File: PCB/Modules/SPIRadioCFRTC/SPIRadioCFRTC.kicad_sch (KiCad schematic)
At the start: 26 parts, among them J1 In, J2 Micro_SD_Card_Det_9pin, Q1 Q_NMOS_GSD, Q2 Q_NMOS_GSD, Q3 Q_NMOS_GSD, U1 DS1390U, U2 nRF24L01P_Module, U3 AMS1117-3.3, Y1 32.767kHz

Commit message: Convert all KiCad to 6.0, clean up libraries, remove files that shouldn't be committed.
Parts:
- J2: symbol SPIRadioCFRTC:Micro_SD_Card_Det_9pin -> KTANE:Micro_SD_Card_Det_9pin
- U1: symbol SPIRadioCFRTC:DS1390U -> KTANE:DS1390U
- U2: symbol SPIRadioCFRTC:nRF24L01P_Module -> KTANE:nRF24L01P_Module
- U3: footprint Package_TO_SOT_SMD:SOT-23 -> Package_TO_SOT_SMD:SOT-223-3_TabPin2
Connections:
- net +3V3 renamed +3.3V
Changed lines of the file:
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@@
     (pin "2")
   )
-  (symbol (lib_id "power:+3.3V") (at 189.23 23.114 0) (unit 1)
+  (symbol (lib_name "+3.3V_2") (lib_id "power:+3.3V") (at 189.23 23.114 0) (unit 1)
     (in_bom yes) (on_board yes)
     (property "Reference" "#PWR01" (id 0) (at 189.23 26.924 0)
@@
     (pin "2")
   )
-  (symbol (lib_id "power:+3.3V") (at 262.89 52.705 0) (mirror y) (unit 1)
+  (symbol (lib_name "+3.3V_8") (lib_id "power:+3.3V") (at 262.89 52.705 0) (mirror y) (unit 1)
     (in_bom yes) (on_board yes)
     (property "Reference" "#PWR014" (id 0) (at 262.89 56.515 0)
@@
     (pin "1")
   )
-  (symbol (lib_id "power:+3.3V") (at 85.852 86.36 0) (mirror y) (unit 1)
+  (symbol (lib_name "+3.3V_1") (lib_id "power:+3.3V") (at 85.852 86.36 0) (mirror y) (unit 1)
     (in_bom yes) (on_board yes)
     (property "Reference" "#PWR028" (id 0) (at 85.852 90.17 0)
@@
     (property "Reference" "U3" (id 0) (at 113.03 77.9485 0))
     (property "Value" "AMS1117-3.3" (id 1) (at 113.03 80.7236 0))
-    (property "Footprint" "Package_TO_SOT_SMD:SOT-23" (id 2) (at 113.03 78.74 0)
+    (property "Footprint" "Package_TO_SOT_SMD:SOT-223-3_TabPin2" (id 2) (at 113.03 78.74 0)
       (effects (font (size 1.27 1.27)) hide)
     )
@@
     (pin "1")
   )
-  (symbol (lib_id "SPIRadioCFRTC:Micro_SD_Card_Det_9pin") (at 49.53 91.44 0) (mirror y) (unit 1)
+  (symbol (lib_id "KTANE:Micro_SD_Card_Det_9pin") (at 49.53 91.44 0) (mirror y) (unit 1)
     (in_bom yes) (on_board yes) (fields_autoplaced)
     (property "Reference" "J2" (id 0) (at 48.895 70.9635 0))
@@
     (pin "1")
   )
-  (symbol (lib_id "power:+3.3V") (at 82.55 24.13 0) (unit 1)
+  (symbol (lib_name "+3.3V_7") (lib_id "power:+3.3V") (at 82.55 24.13 0) (unit 1)
     (in_bom yes) (on_board yes)
     (property "Reference" "#PWR04" (id 0) (at 82.55 27.94 0)
@@
     (pin "3")
   )
-  (symbol (lib_id "SPIRadioCFRTC:nRF24L01P_Module") (at 189.23 39.37 0) (unit 1)
+  (symbol (lib_id "KTANE:nRF24L01P_Module") (at 189.23 39.37 0) (unit 1)
     (in_bom yes) (on_board yes) (fields_autoplaced)
     (property "Reference" "U2" (id 0) (at 191.2494 25.2943 0)
@@
     (pin "1")
   )
-  (symbol (lib_id "power:+3.3V") (at 20.32 78.74 0) (unit 1)
+  (symbol (lib_name "+3.3V_4") (lib_id "power:+3.3V") (at 20.32 78.74 0) (unit 1)
     (in_bom yes) (on_board yes)
     (property "Reference" "#PWR018" (id 0) (at 20.32 82.55 0)
@@
     (pin "2")
   )
-  (symbol (lib_id "power:+3.3V") (at 262.89 25.4 0) (mirror y) (unit 1)
+  (symbol (lib_name "+3.3V_9") (lib_id "power:+3.3V") (at 262.89 25.4 0) (mirror y) (unit 1)
     (in_bom yes) (on_board yes)
     (property "Reference" "#PWR07" (id 0) (at 262.89 29.21 0)
@@
     (pin "1")
   )
-  (symbol (lib_id "power:+3.3V") (at 156.21 78.74 0) (unit 1)
+  (symbol (lib_name "+3.3V_14") (lib_id "power:+3.3V") (at 156.21 78.74 0) (unit 1)
     (in_bom yes) (on_board yes)
     (property "Reference" "#PWR021" (id 0) (at 156.21 82.55 0)
@@
     (pin "1")
   )
-  (symbol (lib_id "power:+3.3V") (at 162.56 78.74 0) (unit 1)
+  (symbol (lib_name "+3.3V_11") (lib_id "power:+3.3V") (at 162.56 78.74 0) (unit 1)
     (in_bom yes) (on_board yes)
     (property "Reference" "#PWR022" (id 0) (at 162.56 82.55 0)
@@
     (pin "2")
   )
-  (symbol (lib_id "power:+3.3V") (at 151.13 26.67 0) (unit 1)
+  (symbol (lib_name "+3.3V_3") (lib_id "power:+3.3V") (at 151.13 26.67 0) (unit 1)
     (in_bom yes) (on_board yes)
     (property "Reference" "#PWR08" (id 0) (at 151.13 30.48 0)
@@
     (pin "1")
   )
-  (symbol (lib_id "SPIRadioCFRTC:DS1390U") (at 115.824 39.37 0) (unit 1)
+  (symbol (lib_id "KTANE:DS1390U") (at 115.824 39.37 0) (unit 1)
     (in_bom yes) (on_board yes) (fields_autoplaced)
     (property "Reference" "U1" (id 0) (at 117.8434 50.3587 0)
@@
     (pin "9")
   )
-  (symbol (lib_id "power:+3.3V") (at 143.51 78.74 0) (unit 1)
+  (symbol (lib_name "+3.3V_13") (lib_id "power:+3.3V") (at 143.51 78.74 0) (unit 1)
     (in_bom yes) (on_board yes)
     (property "Reference" "#PWR019" (id 0) (at 143.51 82.55 0)
@@
     (pin "2")
   )
-  (symbol (lib_id "power:+3.3V") (at 119.634 23.876 0) (unit 1)
+  (symbol (lib_name "+3.3V_6") (lib_id "power:+3.3V") (at 119.634 23.876 0) (unit 1)
     (in_bom yes) (on_board yes)
     (property "Reference" "#PWR03" (id 0) (at 119.634 27.686 0)
@@
     (pin "2")
   )
-  (symbol (lib_id "power:+3.3V") (at 149.86 78.74 0) (unit 1)
+  (symbol (lib_name "+3.3V_12") (lib_id "power:+3.3V") (at 149.86 78.74 0) (unit 1)
     (in_bom yes) (on_board yes)
     (property "Reference" "#PWR020" (id 0) (at 149.86 82.55 0)
@@
     (pin "2")
   )
-  (symbol (lib_id "power:+3.3V") (at 125.73 81.28 0) (unit 1)
+  (symbol (lib_name "+3.3V_10") (lib_id "power:+3.3V") (at 125.73 81.28 0) (unit 1)
     (in_bom yes) (on_board yes)
     (property "Reference" "#PWR027" (id 0) (at 125.73 85.09 0)
@@
     (pin "2")
   )
-  (symbol (lib_id "power:+3.3V") (at 262.89 80.01 0) (mirror y) (unit 1)
+  (symbol (lib_name "+3.3V_5") (lib_id "power:+3.3V") (at 262.89 80.01 0) (mirror y) (unit 1)
     (in_bom yes) (on_board yes)
     (property "Reference" "#PWR025" (id 0) (at 262.89 83.82 0)
@@
     )
     (path "/245afab8-87c2-4797-af78-aa00d5229c94"
-      (reference "U3") (unit 1) (value "AMS1117-3.3") (footprint "Package_TO_SOT_SMD:SOT-23")
+      (reference "U3") (unit 1) (value "AMS1117-3.3") (footprint "Package_TO_SOT_SMD:SOT-223-3_TabPin2")
     )
     (path "/8f7320f7-8fdb-4e68-b345-a40e837bd78d"

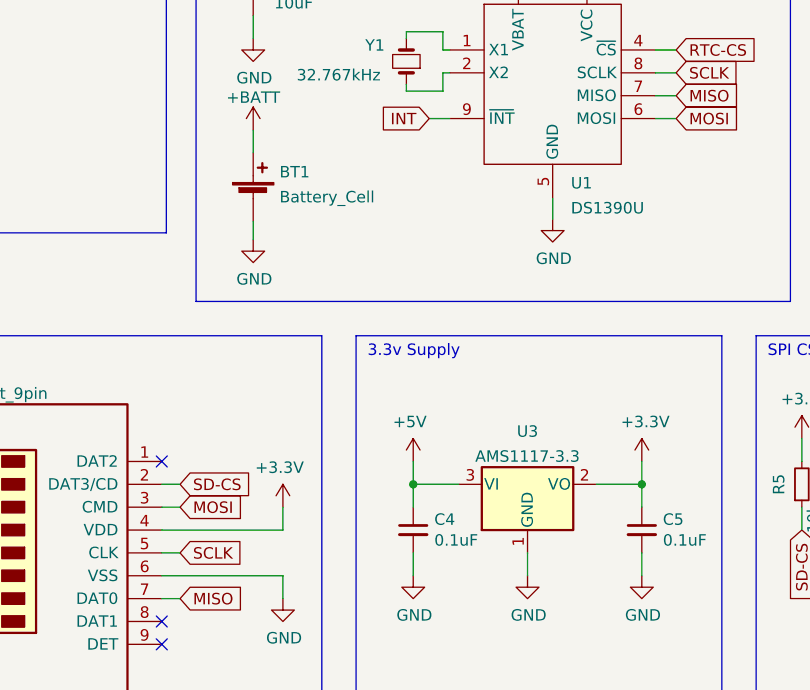
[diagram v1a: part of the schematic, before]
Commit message: Upgrade KiCad files from 6.0 to 7.0.
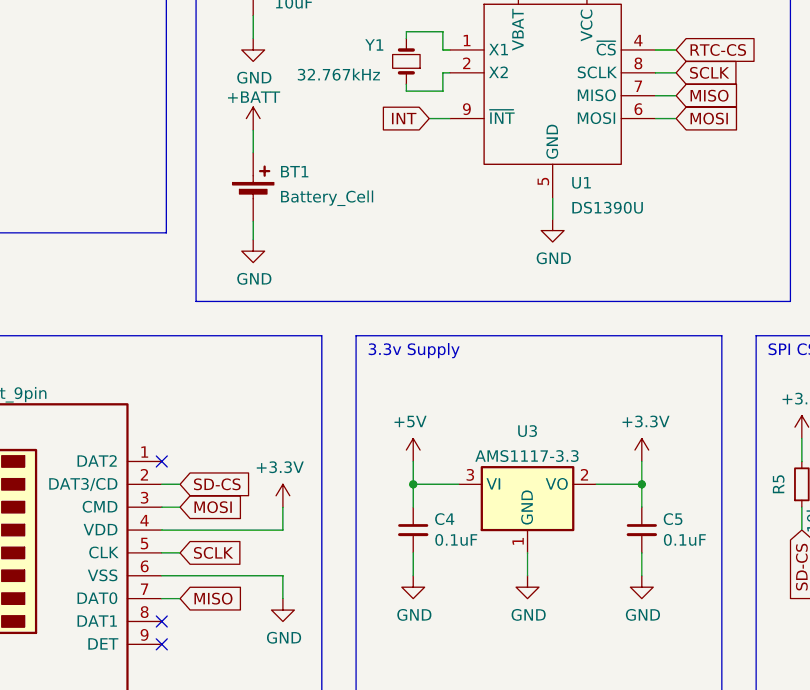
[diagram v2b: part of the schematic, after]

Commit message: First pass of PCB rework.
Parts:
- removed C3: 10uF, Capacitor_SMD:C_0805_2012Metric, symbol Device:C_Small
- removed J2: Micro_SD_Card_Det_9pin, SPIRadioCFRTC:mSDCardSlot, symbol KTANE:Micro_SD_Card_Det_9pin
- removed Q1, Q2, Q3: Q_NMOS_GSD, Package_TO_SOT_SMD:SOT-23, symbol Device:Q_NMOS_GSD
- removed R10, R11, R2, R3, R4, R5, R6, R7, R8, R9: 10k, Resistor_SMD:R_0805_2012Metric, symbol Device:R_Small
- removed U3: AMS1117-3.3, Package_TO_SOT_SMD:SOT-223-3_TabPin2, symbol Regulator_Linear:AMS1117-3.3
- added C6: 10uF, Capacitor_SMD:C_0603_1608Metric, symbol Device:C_Small
- added C7: 0.1uF, Capacitor_SMD:C_0603_1608Metric, symbol Device:C_Small
- added H1: MountingHole, MountingHole:MountingHole_3.2mm_M3, symbol Mechanical:MountingHole
- added J2: ESP32, Connector:Tag-Connect_TC2030-IDC-NL_2x03_P1.27mm_Vertical, symbol Connector_Generic:Conn_02x03_Odd_Even
- added U4: ESP32-WROOM-32, RF_Module:ESP32-WROOM-32U, symbol RF_Module:ESP32-WROOM-32U
- BT1: footprint SPIRadioCFRTC:CellHolder -> KTANE:CellHolder
- C1, C2: footprint Capacitor_SMD:C_0805_2012Metric -> Capacitor_SMD:C_0603_1608Metric
- C4: value 0.1uF -> 22uF; footprint Capacitor_SMD:C_0805_2012Metric -> Capacitor_SMD:C_0603_1608Metric
- C5: value 0.1uF -> 47uF; footprint Capacitor_SMD:C_0805_2012Metric -> Capacitor_SMD:C_0603_1608Metric
- J1: footprint Custom:PinHeader_2x08_P2.54mm_Vertical-Centered -> KTANE:PinHeader_2x08_P2.54mm_Vertical-Centered
- R1: footprint Resistor_SMD:R_0805_2012Metric -> Resistor_SMD:R_0603_1608Metric
- U2: footprint SPIRadioCFRTC:NRF24L01P-Module -> KTANE:NRF24L01P-Module
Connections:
- net IN-MISO is gone; now on net +5V: J1.2 (Pin_2)
- net IN-MOSI is gone; now on net +3.3V: J1.4 (Pin_4)
- net SD-CS is gone; now on net SPI-CIPO: J1.14 (Pin_14)
- net +3.3V: now also C4.1, R1.1, C7.1, J2.2 (Pin_2), U4.2 (VDD)
- net +5V: no longer C4.1, J1.11 (Pin_11), J1.13 (Pin_13), J1.15 (Pin_15), J1.9 (Pin_9), R1.2
- net GND: now also J1.16 (Pin_16), C6.2, C7.2, J2.3 (Pin_3), U4.1 (GND), U4.15 (GND), U4.38 (GND), U4.39 (GND); no longer J1.1 (Pin_1), J1.3 (Pin_3), J1.5 (Pin_5), J1.7 (Pin_7)
- net NF24-CE: now also J1.7 (Pin_7); no longer J1.10 (Pin_10)
- net NF24-CS: now also J1.5 (Pin_5); no longer J1.12 (Pin_12)
- net RTC-CS: now also J1.1 (Pin_1); no longer J1.16 (Pin_16)
- net IN-SCLK renamed I2C-CLK
- net I2C-CLK: no longer R1.1
- removed net INT: J1.8 (Pin_8), U1.9 (~{INT}), U2.7 (~{IRQ})
- net MISO renamed SPI-CIPO
- net SPI-CIPO: now also U4.14 (IO12)
- net MOSI renamed SPI-COPI
- net SPI-COPI: now also J1.12 (Pin_12), U4.16 (IO13)
- net SCLK renamed SPI-CLK
- net SPI-CLK: now also J1.10 (Pin_10), U4.13 (IO14)
- new net BOOT0: J2.6 (Pin_6), U4.25 (IO0)
- new net EN: C6.1, J2.4 (Pin_4), R1.2, U4.3 (EN)
- new net ESP32-CS: J1.11 (Pin_11), U4.23 (IO15)
- new net ESP32-RX: J1.13 (Pin_13), J2.5 (Pin_5), U4.34 (RXD0/IO3)
- new net ESP32-TX: J1.15 (Pin_15), J2.1 (Pin_1), U4.35 (TXD0/IO1)
- new net I2C-DAT: J1.8 (Pin_8)
- new net NF24-INT: J1.9 (Pin_9), U2.7 (~{IRQ})
- new net RTC-INT: J1.3 (Pin_3), U1.9 (~{INT})
- no-connect marks 3 -> 25
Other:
- note added: "ESP32"
- note added: "Mounting Hole"
- note removed: "3.3v Supply"
- note removed: "MicroSD Card"
- note removed: "SPI CS/Int Pull Up"
- note removed: "SPI Level Shift"
- moved on the sheet: BT1, C1, C2, J1, U1, U2, Y1
